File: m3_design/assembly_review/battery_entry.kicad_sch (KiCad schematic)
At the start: 26 parts, among them J1 DB125-3.5-2P-GN-S, J400 BM02B-GHS-TBT(LF)(SN), U9 TPS259470LRPWR

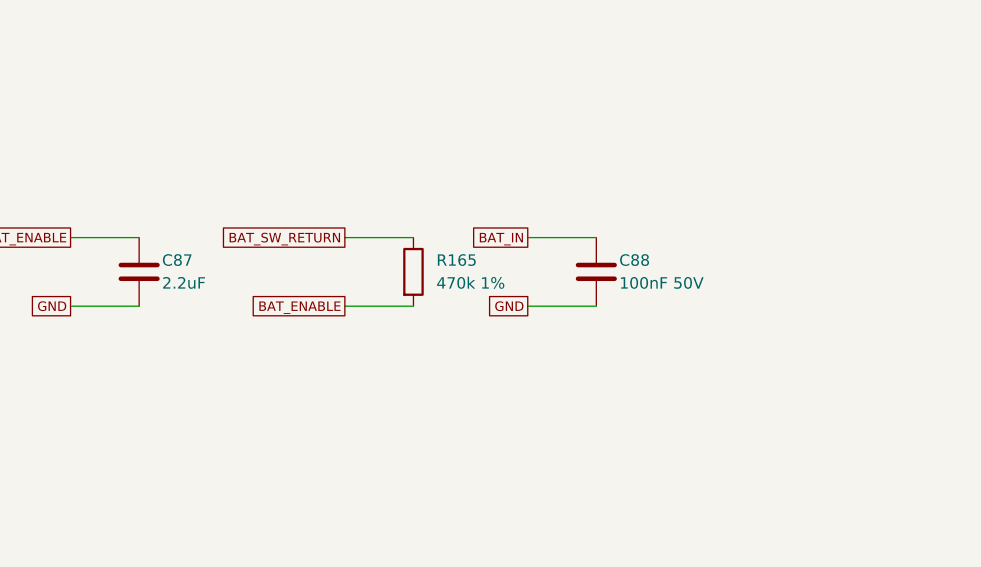
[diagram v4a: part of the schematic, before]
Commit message: Finish R10 round 9 Minor fix pass
Complete the interrupted generator rebuild and apply the recorded round 9
Minor fixes: capacitor labels, cold-screen ordering, debugger instructions,
local route cleanups, gate fault detection and explicit R10 procurement limits.
Refresh the board-bound fabrication, supplier and validation records.

Round 9 reviewed 8bccb07: 0 Critical, 0 Major, 21 Minor groups. Round 10 will
freshly review this committed fix pass, including every changed CAD item.

Board SHA-256: b337fe63c258c85ba4120e75ad018afa0c22241f8bc21a4172787cf2887208d9
Board: 46 x 90 mm, 2366509 bytes. Two COMPLETE builds pass; all 21 generated
CAD and binding files are byte-identical.

Unskipped tools/check.sh: exit 0.
DRC violations 0; unconnected 0; schematic parity 0; ERC 0.
Metadata / 3D, silk, fit / plate, all 33 R10 rules, routing hygiene, actuator
contract and current 5-output fabrication manifest: OK.
Self-tests: shell 4, procurement 19, fit 24, paste 5, routing 59, R10 140;
3 NumPy cases rerun successfully, no unresolved skips. Hot-plug: 2304/2304
required cases pass (simulation / Inference).

Fab export, required fitting, orientation and paste pass: 215 CPL rows,
82 BOM codes. Fresh supplier/procurement checks correctly FAIL the known
$84.43 versus $84.41 cap and R430/U4 stock shortages; 46 Extended codes.
OQ-3 and final deviation acceptance remain pending. No firmware, bench,
installed RF immunity, physical fit, assembly-process or flight result claimed.

Evidence: docs/R10_VALIDATION.md and sources/r10_review/round9_fix_validation.json
and round9_fix_check.txt under m3_design/assembly_review. Native headless
KiCad environment uses the external D-R1-05 mouse-query workaround only;
repository gates and CAD rules are unchanged by that workaround.

Co-Authored-By: Claude Opus 5.5 <noreply@anthropic.com>
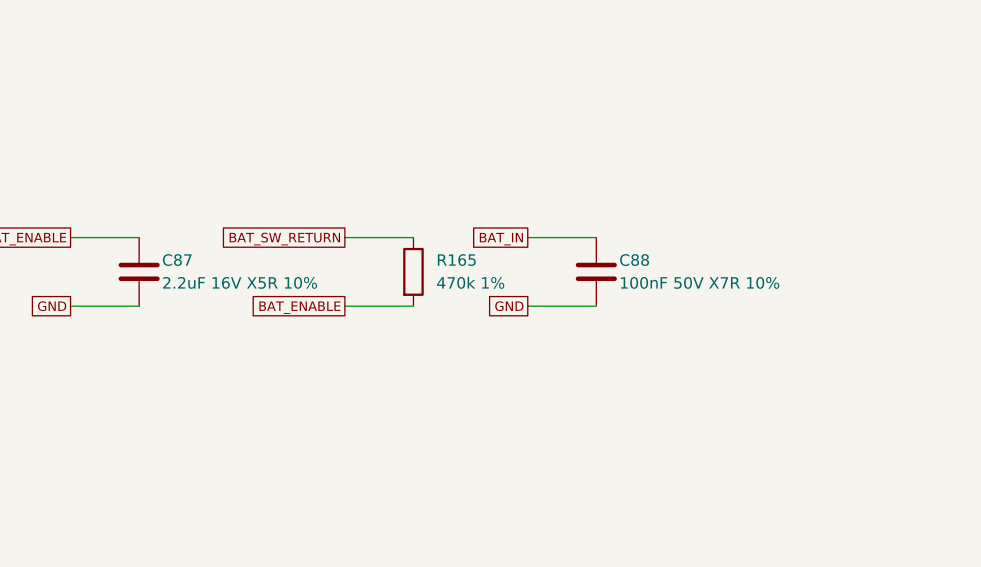
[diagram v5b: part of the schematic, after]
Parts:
- C87: value 2.2uF -> 2.2uF 16V X5R 10%
- C88: value 100nF 50V -> 100nF 50V X7R 10%
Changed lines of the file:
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@@
 					(size 1.27 1.27))
 				(justify left)))
-		(property "Value" "2.2uF"
+		(property "Value" "2.2uF 16V X5R 10%"
 			(at 342.9 123.19 0)
 			(effects
@@
 					(size 1.27 1.27))
 				(justify left)))
-		(property "Value" "100nF 50V"
+		(property "Value" "100nF 50V X7R 10%"
 			(at 393.7 123.19 0)
 			(effects
